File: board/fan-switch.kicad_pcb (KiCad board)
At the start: 2 copper layers, 50 x 35 mm, 16 parts, among them J1 12V, J2 GND, J3 M+, J4 M-, J5 PROG, Q1 BXT420N03M, U1 ESP32-C3-WROOM-02, U2 LM1117-3.3

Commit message: 2.1
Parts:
- removed the J5 at (143.5, 111.0)
- added A1: 31mm, Drake:Wire antena 2.4GHz, F.Cu at (131.0, 110.0)
- added C4: 10u, Capacitor_SMD:C_0805_2012Metric, F.Cu at (122.0, 105.0)
- added C5: 100n, Capacitor_SMD:C_0805_2012Metric, F.Cu at (116.0, 122.0)
- added C6: 100n, Capacitor_SMD:C_0805_2012Metric, F.Cu at (112.0, 122.0)
- added J3: TX, Connector_PinHeader_2.54mm:PinHeader_1x01_P2.54mm_Vertical, F.Cu at (107.0, 112.0)
- added U3: PY32F003W1xSx, Package_SO:SOIC-16_3.9x9.9mm_P1.27mm, F.Cu at (114.0, 115.0)
- added X1: SWD, Drake:SWD, F.Cu at (121.0, 116.0)
- added Y1: 16MHz, Crystal:Crystal_SMD_3225-4Pin_3.2x2.5mm, F.Cu at (133.0, 120.0)
- C1: footprint Capacitor_SMD:C_0805_2012Metric_Pad1.18x1.45mm_HandSolder -> Capacitor_SMD:C_0805_2012Metric
- C2: value 47u -> 1u; footprint Capacitor_SMD:C_0805_2012Metric_Pad1.18x1.45mm_HandSolder -> Capacitor_SMD:C_0805_2012Metric
- C3: value 47u -> 100n; footprint Capacitor_SMD:C_0805_2012Metric_Pad1.18x1.45mm_HandSolder -> Capacitor_SMD:C_0805_2012Metric
- Q1: value BXT420N03M -> AO3400A
- R3: value 270R -> 330R
- U1: value ESP32-C3-WROOM-02 -> LM1117MP-3.3; footprint Espressif:ESP32-C3-WROOM-02 -> Package_TO_SOT_SMD:SOT-223-3_TabPin2
- U2: value LM1117-3.3 -> PAN2110P0AA; footprint Package_TO_SOT_SMD:SOT-223-3_TabPin2 -> Package_SO:SOIC-8_3.9x4.9mm_P1.27mm
- moved U2 23.2 mm to (131.0, 115.0), turned to 0 degrees
- moved C1 17.2 mm to (122.0, 101.0)
- moved D2 16.5 mm to (107.0, 116.0)
- moved R3 16.5 mm to (107.0, 120.0)
- moved C2 15.5 mm to (129.2, 121.0), turned to 0 degrees
- moved C3 12.3 mm to (129.2, 119.0), turned to 0 degrees
- moved U1 10.0 mm to (115.0, 103.0), turned to 180 degrees
- moved Q1 5.10 mm to (142.0, 112.0), turned to 90 degrees
- moved R2 5.10 mm to (142.0, 116.0)
- moved R1 5.00 mm to (142.0, 119.0)
- renumbered J3 to J4, J4 to J5, R2 to R1, R1 to R2
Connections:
- U1 pad 1: +3V3 -> GND
- U1 pad 3: /LED -> +12V
- U2 pad 1: GND -> /~{RF_CS}
- U2 pad 2: +3V3 -> /RF_SCK
- U2 pad 3: +12V -> /RF_DATA
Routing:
- net +3V3: track 21.5 -> 71.3 mm, vias 6 -> 0
- net +12V: track 68.4 -> 45.7 mm
- net GND: track 0.00 -> 20.2 mm, vias 0 -> 38
- net /~{RF_CS}: track 0.00 -> 19.5 mm
- net /GATE: track 27.0 -> 43.8 mm, vias 2 -> 0
- net /USB_D+: track 15.1 -> 0.00 mm
- net /RF_DATA: track 0.00 -> 13.6 mm
- net /RF_SCK: track 0.00 -> 13.6 mm
- net Net-(U3-PF0/PF2-NRST): track 0.00 -> 10.5 mm
- net /USB_D-: track 8.53 -> 0.00 mm
- net Net-(D1-A): track 18.2 -> 11.0 mm
- net /TX: track 0.00 -> 6.03 mm
- net Net-(U2-XC1): track 0.00 -> 5.79 mm
- net /SWCLK: track 0.00 -> 5.43 mm
- net /SWDIO: track 0.00 -> 5.20 mm
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- added copper zone on B.Cu, net GND
- removed copper zone on B.Cu, net +3V3
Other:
- board text added: "Fan Switch v2.1"
- board text removed: "Fan Switch v1.0"

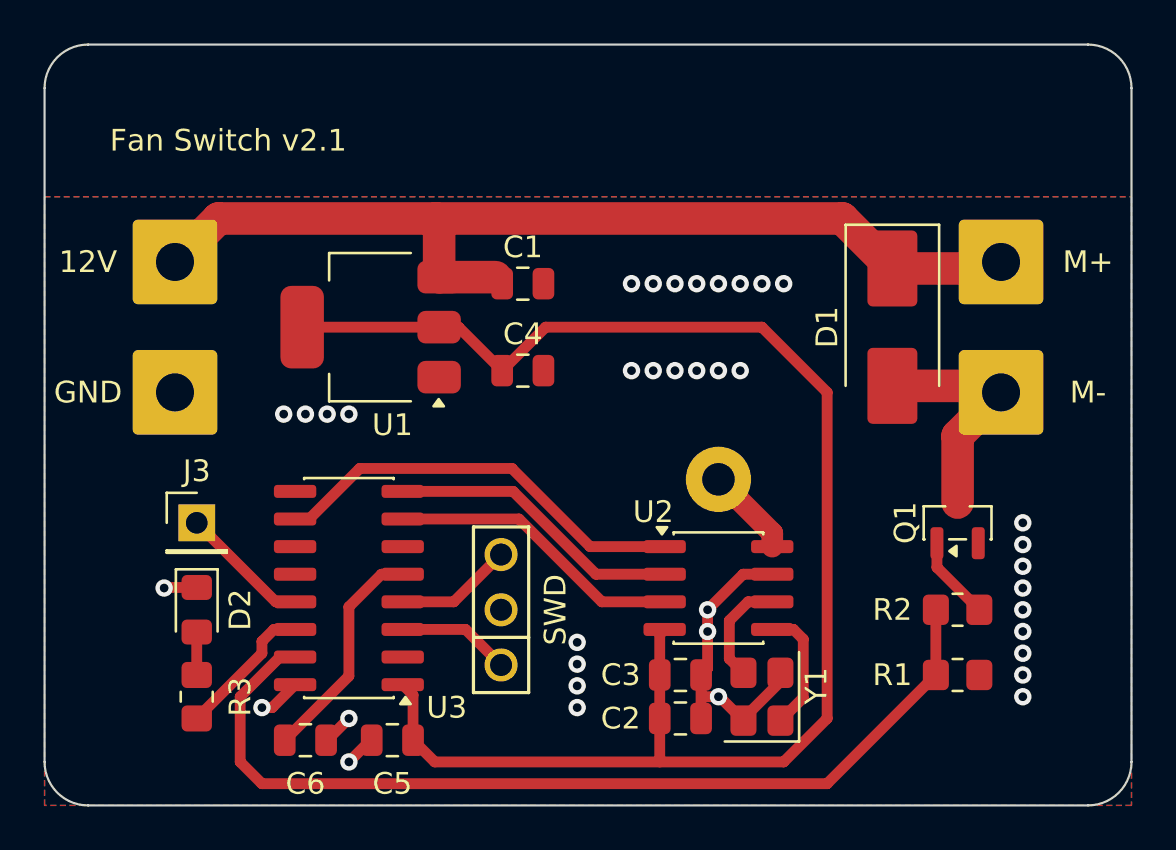
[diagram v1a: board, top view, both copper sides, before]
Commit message: Refactor fan control and update schematic
- Updated fan PWM configuration in main.go to use TIM14 on PB1 with a frequency of 50 kHz.
- Added setupFanPWM and setFanDuty methods to manage fan speed via PWM.
- Adjusted pin assignments for SPI communication.
- Modified the schematic to reflect new pin locations and updated component positions.
- Changed Makefile to include new commands for project management.
- Updated test-hub.go with new UID and Key values for the fan device.
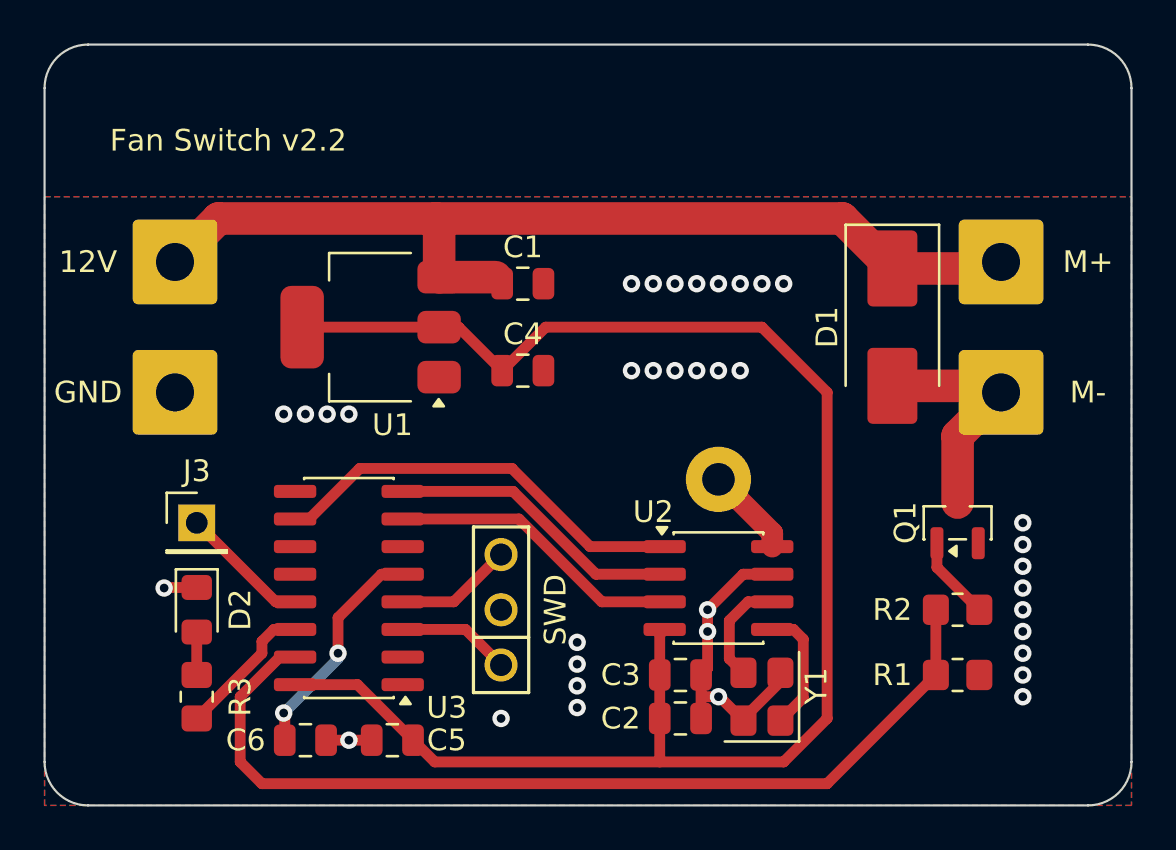
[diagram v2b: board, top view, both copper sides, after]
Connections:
- U3 pad 1: +3V3 -> GND
- U3 pad 16: GND -> +3V3
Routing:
- net +3V3: track 71.3 -> 75.0 mm
- net GND: track 20.2 -> 17.4 mm, vias 38 -> 37
- net Net-(U3-PF0/PF2-NRST): vias 0 -> 2
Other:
- board text added: "Fan Switch v2.2"
- board text removed: "Fan Switch v2.1"
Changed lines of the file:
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@@
 		(tags "capacitor")
 		(property "Reference" "C5"
-			(at 0 -2 0)
+			(at -2.5 0 0)
 			(layer "F.SilkS")
 			(effects
@@
 			(layers "F.Cu" "F.Mask" "F.Paste")
 			(roundrect_rratio 0.25)
-			(net 3 "+3V3")
+			(net 2 "GND")
 			(pinfunction "VSS")
 			(pintype "power_in")
@@
 			(layers "F.Cu" "F.Mask" "F.Paste")
 			(roundrect_rratio 0.25)
-			(net 2 "GND")
+			(net 3 "+3V3")
 			(pinfunction "VCC")
 			(pintype "power_in")
@@
 		(tags "capacitor")
 		(property "Reference" "C6"
-			(at 0 2 0)
+			(at -2.75 0 0)
 			(layer "F.SilkS")
 			(effects
@@
 		(layer "Edge.Cuts")
 	)
-	(gr_text "Fan Switch v2.1"
+	(gr_text "Fan Switch v2.2"
 		(at 103 95 0)
 		(layer "F.SilkS")
@@
 	)
 	(segment
-		(start 115.05 122)
-		(end 115 122)
-		(width 0.5)
-		(layer "F.Cu")
-		(net 2)
-	)
-	(segment
-		(start 115 122)
-		(end 114 123)
+		(start 107 114.975)
+		(end 105.525 114.975)
 		(width 0.5)
 		(layer "F.Cu")
@@
 	)
 	(segment
-		(start 107 114.975)
-		(end 105.525 114.975)
+		(start 115.05 122)
+		(end 112.95 122)
 		(width 0.5)
 		(layer "F.Cu")
@@
 	)
 	(segment
-		(start 110.47 120.5)
-		(end 111.525 119.445)
-		(width 0.5)
-		(layer "F.Cu")
-		(net 2)
-	)
-	(segment
-		(start 110 120.5)
-		(end 110.47 120.5)
-		(width 0.5)
-		(layer "F.Cu")
-		(net 2)
-	)
-	(segment
 		(start 105.525 114.975)
 		(end 105.5 115)
@@
 	)
 	(segment
-		(start 112.95 122)
-		(end 113 122)
-		(width 0.5)
-		(layer "F.Cu")
-		(net 2)
-	)
-	(segment
-		(start 113 122)
-		(end 114 121)
-		(width 0.5)
-		(layer "F.Cu")
-		(net 2)
-	)
-	(segment
 		(start 133.475 114.365)
 		(end 132.135 114.365)
@@
 	)
 	(via
-		(at 114 121)
+		(at 114 122)
 		(size 0.8)
 		(drill 0.4)
@@
 	)
 	(via
-		(at 114 123)
-		(size 0.8)
-		(drill 0.4)
-		(layers "F.Cu" "B.Cu")
-		(free yes)
-		(net 2)
-	)
-	(via
 		(at 145 118)
 		(size 0.8)
@@
 	)
 	(via
-		(at 110 120.5)
+		(at 121 121)
 		(size 0.8)
 		(drill 0.4)
@@
 	)
 	(segment
-		(start 119.05 103)
-		(end 121.05 105)
-		(width 0.5)
-		(layer "F.Cu")
-		(net 3)
-	)
-	(segment
-		(start 116.95 119.92)
-		(end 116.475 119.445)
+		(start 117.95 123)
+		(end 116.95 122)
 		(width 0.5)
 		(layer "F.Cu")
@@
 	)
 	(segment
-		(start 116.95 122)
-		(end 116.95 119.92)
+		(start 119.05 103)
+		(end 121.05 105)
 		(width 0.5)
 		(layer "F.Cu")
@@
 	)
 	(segment
-		(start 117.95 123)
-		(end 116.95 122)
+		(start 114.395 119.445)
+		(end 111.525 119.445)
 		(width 0.5)
 		(layer "F.Cu")
@@
 	)
 	(segment
+		(start 116.95 122)
+		(end 114.395 119.445)
+		(width 0.5)
+		(layer "F.Cu")
+		(net 3)
+	)
+	(segment
 		(start 128.3 117.13)
 		(end 128.525 116.905)
@@
 	)
 	(segment
-		(start 115.500001 114.365)
-		(end 114 115.865001)
+		(start 116.475 114.365)
+		(end 115.500001 114.365)
 		(width 0.5)
 		(layer "F.Cu")
@@
 	)
 	(segment
-		(start 114 115.865001)
-		(end 114 119.05)
+		(start 111.05 120.8)
+		(end 111 120.75)
 		(width 0.5)
 		(layer "F.Cu")
@@
 	)
 	(segment
-		(start 116.475 114.365)
-		(end 115.500001 114.365)
+		(start 111.05 122)
+		(end 111.05 120.8)
+		(width 0.5)
+		(layer "F.Cu")
+		(net 10)
+	)
+	(segment
+		(start 115.500001 114.365)
+		(end 113.5 116.365001)
 		(width 0.5)
 		(layer "F.Cu")
@@
 	)
 	(segment
-		(start 114 119.05)
-		(end 111.05 122)
+		(start 113.5 116.365001)
+		(end 113.5 118)
 		(width 0.5)
 		(layer "F.Cu")
 		(net 10)
 	)
+	(via
+		(at 113.5 118)
+		(size 0.8)
+		(drill 0.4)
+		(layers "F.Cu" "B.Cu")
+		(net 10)
+	)
+	(via
+		(at 111 120.75)
+		(size 0.8)
+		(drill 0.4)
+		(layers "F.Cu" "B.Cu")
+		(net 10)
+	)
+	(segment
+		(start 113.5 118.25)
+		(end 111 120.75)
+		(width 0.5)
+		(layer "B.Cu")
+		(net 10)
+	)
+	(segment
+		(start 113.5 118)
+		(end 113.5 118.25)
+		(width 0.5)
+		(layer "B.Cu")
+		(net 10)
+	)
